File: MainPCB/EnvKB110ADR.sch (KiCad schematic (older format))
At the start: 246 parts, among them SW1 Boot Mode, SW2 Reset Switch, U1 XC6206PxxxMR, U2 STM32F411CEUx, Y1 3225_4P 32.768khz

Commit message: Converted board from STM32F411CEU6 to RP2040
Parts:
- removed C1, C2, C3, C4: 100nf capacitor, Capacitor_SMD:C_0402_1005Metric, symbol Device:C_Small
- removed C10, C9: 0402 22pF, Capacitor_SMD:C_0402_1005Metric, symbol Device:C_Small
- removed C5, C6: 1uf capacitor, Capacitor_SMD:C_0402_1005Metric, symbol Device:C_Small
- removed C7, C8: 100nf 0402, Capacitor_SMD:C_0402_1005Metric, symbol Device:C_Small
- removed R1: 1.5K 0402, Resistor_SMD:R_0402_1005Metric, symbol Device:R_Small
- removed R2: 5.1K 0402, Resistor_SMD:R_0402_1005Metric, symbol Device:R_Small
- removed R3, R4: 22ohm, Resistor_SMD:R_0402_1005Metric, symbol Device:R_Small
- removed R7: 10K 0402, Resistor_SMD:R_0402_1005Metric, symbol Device:R_Small
- removed SW1: Boot Mode, Button_Switch_SMD:Panasonic_EVQPUJ_EVQPUA, symbol Switch:SW_Push
- removed SW2: Reset Switch, Button_Switch_SMD:Panasonic_EVQPUJ_EVQPUA, symbol Switch:SW_Push
- removed U1: XC6206PxxxMR, Package_TO_SOT_SMD:SOT-23, symbol Regulator_Linear:XC6206PxxxMR
- removed U2: STM32F411CEUx, Package_DFN_QFN:QFN-48-1EP_7x7mm_P0.5mm_EP5.6x5.6mm, symbol MCU_ST_STM32F4:STM32F411CEUx
- added C1: 10uf 0603 6.3V, Capacitor_SMD:C_0603_1608Metric, symbol Device:C
- added C10, C3: 1uf 0402, Capacitor_SMD:C_0402_1005Metric, symbol Device:C
- added C11, C13, C14, C15, C16, C18, C5, C6, C7, C8: 100nf 0402, Capacitor_SMD:C_0402_1005Metric, symbol Device:C
- added C17, C4, CBP1: 10uf 0402, Capacitor_SMD:C_0402_1005Metric, symbol Device:C
- added C19, C2: 22pf 0402, Capacitor_SMD:C_0402_1005Metric, symbol Device:C
- added D1: 1N4002W, Diode_SMD:D_SOD-123, symbol Device:D_Schottky
- added D3: LED_0603, LED_SMD:LED_0603_1608Metric, symbol Device:LED
- added FLASH1: W25Q128JVPIQ, Package_SON:WSON-8-1EP_6x5mm_P1.27mm_EP3.4x4mm, symbol W25Q256JVEIQ_TR:W25Q256JVEIQ_TR
- added J2: EVQPU, Button_Switch_SMD:Panasonic_EVQPUJ_EVQPUA, symbol Switch:SW_Push
- added J5: Conn_01x03_Male, Connector_PinHeader_2.54mm:PinHeader_1x03_P2.54mm_Horizontal, symbol Connector_Generic:Conn_01x03
- added PWRLED1: LED_0805, LED_SMD:LED_0805_2012Metric, symbol Device:LED
- added R1, R11: 1K 0402 Resistor, Capacitor_SMD:C_0402_1005Metric, symbol Device:R
- added R10: 1 0402, Resistor_SMD:R_0402_1005Metric, symbol Device:R_Small
- added R12: 1K 0402 Resistor, Resistor_SMD:R_0402_1005Metric, symbol Device:R
- added R2: DNF, Capacitor_SMD:C_0402_1005Metric, symbol Device:R
- added R3, R4: 27 0402 Resistor, Resistor_SMD:R_0402_1005Metric, symbol Device:R
- added R7: 100K 0402 resistor, Resistor_SMD:R_0402_1005Metric, symbol Device:R
- added R8: 470 0402 Resistor, Resistor_SMD:R_0402_1005Metric, symbol Device:R
- added R9: 200 0603, Resistor_SMD:R_0603_1608Metric, symbol Device:R_Small
- added RSW1: EVQPU, Button_Switch_SMD:Panasonic_EVQPUJ_EVQPUA, symbol Device:Jumper_NO_Small
- added TP1, TP2, TP3, TP4, TP5, TP6, TP7, TP8: TestPoint, TestPoint:TestPoint_Pad_D1.0mm, symbol Connector:TestPoint
- added U1: TLV75533PDBVR, Package_TO_SOT_SMD:SOT-23-5, symbol Regulator_Linear:AP131-15
- added U3: RP2040, RP2040_minimal:RP2040-QFN-56, symbol MCU_RaspberryPi_RP2040:RP2040
- R5: LCSC (none) -> (none)
- R6: value 100k 0402 -> 5.1K 0402; LCSC (none) -> (none)
- USB1: value HRO-TYPE-C-31-M-12 -> TYPE-C-31-M-12; footprint Type-C:HRO-TYPE-C-31-M-12-Assembly -> HRO-TYPE-C31-M-12:HRO-TYPE-C-31-M-12; LCSC (none) -> C165948
- Y1: value 3225_4P 32.768khz -> 3225_4P; LCSC (none) -> (none)
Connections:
- net boot0 is gone; now on net GND: R6.1
- net +3V3: now also C10.1, C11.1, C13.1, C14.1, C15.1, C16.1, C17.1, C18.1, C4.1, C5.1, C8.1, FLASH1.8 (VCC), R10.2, R2.1, R9.1, TP6.1, TP8.1, U1.5 (OUT), U3.1 (IOVDD), U3.10 (IOVDD), U3.22 (IOVDD), U3.33 (IOVDD), U3.42 (IOVDD), U3.43 (ADC_AVDD), U3.44 (VREG_IN), U3.48 (USB_VDD), U3.49 (IOVDD)
- net GND: now also C1.2, C10.2, C11.2, C13.2, C14.2, C15.2, C16.2, C17.2, C18.2, C19.1, C2.1, C3.2, C4.2, C5.2, C6.2, C7.2, C8.2, CBP1.2, D3.1 (K), FLASH1.4 (GND), FLASH1.9 (EXP), J2.2, J5.2 (Pin_2), PWRLED1.1 (K), RSW1.1, TP3.1, U1.2 (GND), U3.19 (TESTEN), U3.57 (GND); no longer R6.2
- net VBUS: now also D1.2 (A), R12.2, TP4.1
- net XIN: now reaches Y1.1
- net XIN: now also C2.2, U3.20 (XIN)
- net at Y1.3: now also C19.2, R11.2
- net at USB1.10 (CC2): now also R6.2; no longer R5.2
- net at USB1.4 (CC1): now also R5.2
- net D+ renamed USB_D+
- net USB_D+: now also R3.1, TP1.1
- net D- renamed USB_D-
- net USB_D-: now also R4.1, TP2.1
- new net: R4.2, U3.46 (USB_DM)
- new net: R3.2, U3.47 (USB_DP)
- new net: D3.2 (A), R8.1
- new net: CBP1.1, U1.4 (BP)
- new net: PWRLED1.2 (A), R12.1
- new net +1V1: C3.1, C6.1, C7.1, TP7.1, U3.23 (DVDD), U3.45 (VREG_VOUT), U3.50 (DVDD)
- new net 3V3_EN: R7.1, U1.3 (EN)
- new net ADC_VREF: R10.1, R9.2
- new net GPIO0: U3.2 (GPIO0)
- new net GPIO1: U3.3 (GPIO1)
- new net GPIO10: U3.13 (GPIO10)
- new net GPIO11: U3.14 (GPIO11)
- new net GPIO12: U3.15 (GPIO12)
- new net GPIO13: U3.16 (GPIO13)
- new net GPIO14: U3.17 (GPIO14)
- new net GPIO15: U3.18 (GPIO15)
- new net GPIO16: U3.27 (GPIO16)
- new net GPIO17: U3.28 (GPIO17)
- new net GPIO18: U3.29 (GPIO18)
- new net GPIO19: U3.30 (GPIO19)
- new net GPIO2: U3.4 (GPIO2)
- new net GPIO20: U3.31 (GPIO20)
- new net GPIO21: U3.32 (GPIO21)
- new net GPIO22: U3.34 (GPIO22)
- new net GPIO23: U3.35 (GPIO23)
- new net GPIO24: U3.36 (GPIO24)
- new net GPIO25: R8.2, U3.37 (GPIO25)
- new net GPIO26_ADC0: U3.38 (GPIO26_ADC0)
- new net GPIO27_ADC1: U3.39 (GPIO27_ADC1)
- new net GPIO28_ADC2: U3.40 (GPIO28_ADC2)
- new net GPIO29_ADC3: U3.41 (GPIO29_ADC3)
- new net GPIO3: U3.5 (GPIO3)
- new net GPIO4: U3.6 (GPIO4)
- new net GPIO5: U3.7 (GPIO5)
- new net GPIO6: U3.8 (GPIO6)
- new net GPIO7: U3.9 (GPIO7)
- new net GPIO8: U3.11 (GPIO8)
- new net GPIO9: U3.12 (GPIO9)
- new net QSPI_SCLK: FLASH1.6 (CLK), U3.52 (QSPI_SCLK)
- new net QSPI_SD0: FLASH1.5 (DI(IO0)), U3.53 (QSPI_SD0)
- new net QSPI_SD1: FLASH1.2 (DO(IO1)), U3.55 (QSPI_SD1)
- new net QSPI_SD2: FLASH1.3 (IO2), U3.54 (QSPI_SD2)
- new net QSPI_SD3: FLASH1.7 (IO3), U3.51 (QSPI_SD3)
- new net QSPI_SS: FLASH1.1 (~CS), R1.1, R2.2, U3.56 (QSPI_SS)
- new net RUN: RSW1.2, U3.26 (RUN)
- new net SWCLK: J5.1 (Pin_1), U3.24 (SWCLK)
- new net SWD: J5.3 (Pin_3), U3.25 (SWD)
- new net VSYS: C1.1, D1.1 (K), R7.2, TP5.1, U1.1 (IN)
- new net XOUT: R11.1, U3.21 (XOUT)
- new net ~USB_BOOT: J2.1, R1.2
- no-connect marks 7 -> 3
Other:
- note added: "2x 5.1K Resistors on the CC pins will = 5V@1.5A\nthis is the recomended default config for type-c"
- note added: "Crystal"
- note added: "D1 NEEDS to be 0omh resistor or 1N4002 diode"
- note added: "DO.NOT.FIT"
- note added: "Flash"
- note added: "GD25Q40CEIGR is compatible and often stocked by JLC"
- note added: "Im pretty sure a lot of these W25QXXX Chips are pin compatible\nDont quote me on that"
- note added: "Im unsure if the RP2040 can function with flash larger than 128Mb"
- note added: "KoreanHROParts \nUSB_C_Receptacle_HRO_TYPE-C-31-M-12"
- note added: "MAKE SURE THIS LINE is ran off of pin43\nor close to pin43"
- note added: "Make sure C10 is close to pin 44 of RP2040"
- note added: "Make sure C3 is close to pin 45 of RP2040"
- note added: "Make sure R3 and R4 are close to RP2040"
- note added: "Only fit cBP1 if you have selected an \nalternate voltage regulator\n\nTLV75533PDBVR does not."
- note added: "Pin 9 technically doesnt exist\nits the main central contact under\nthe chip for heat dicipation"
- note added: "RP2040 supports 1MHz to 15MHz"
- note added: "Test points"
- note added: "These decoupling capacitors are meant\nto be put close by each 3.3V pin of the RP2040"
- note added: "USB/POWER"
- note added: "place one by the CPU\nand one by the regulator\n(3.3V Test points)"
- note added: "this is for factory testing\nalways pull this to ground"
- note removed: "these capacitors should all be placed\n near the power pin of the STM32"
- note removed: "unsure what this pullup resistor is for\nbut its used in some MCU boards so lets copy it"
- moved on the sheet: D_100, D_101, D_102, D_103, D_104, D_105, D_106, D_107, D_108, D_109, D_110, D_111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

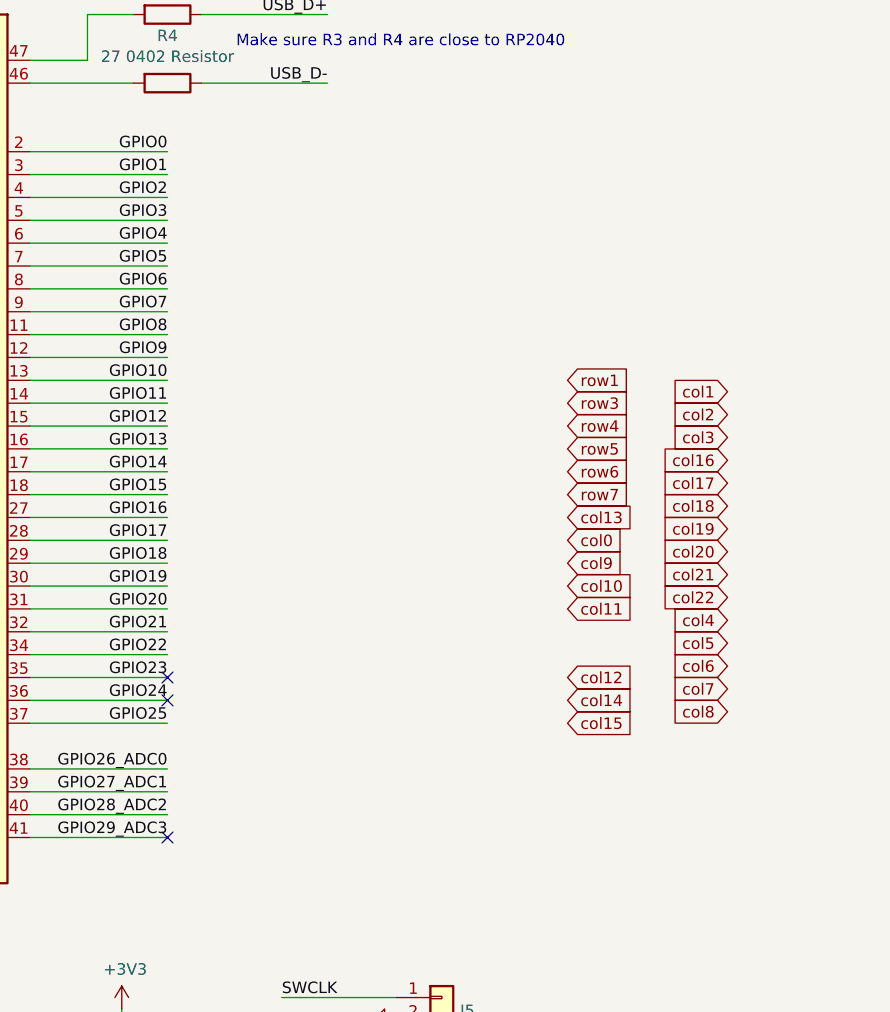
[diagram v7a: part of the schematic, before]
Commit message: wired up all the traces required to make the keyboard functional.
However this means you can no longer use the Rpi pico firmware with this and needs a custom compiled firmware to utilize the normally unavailable pins,
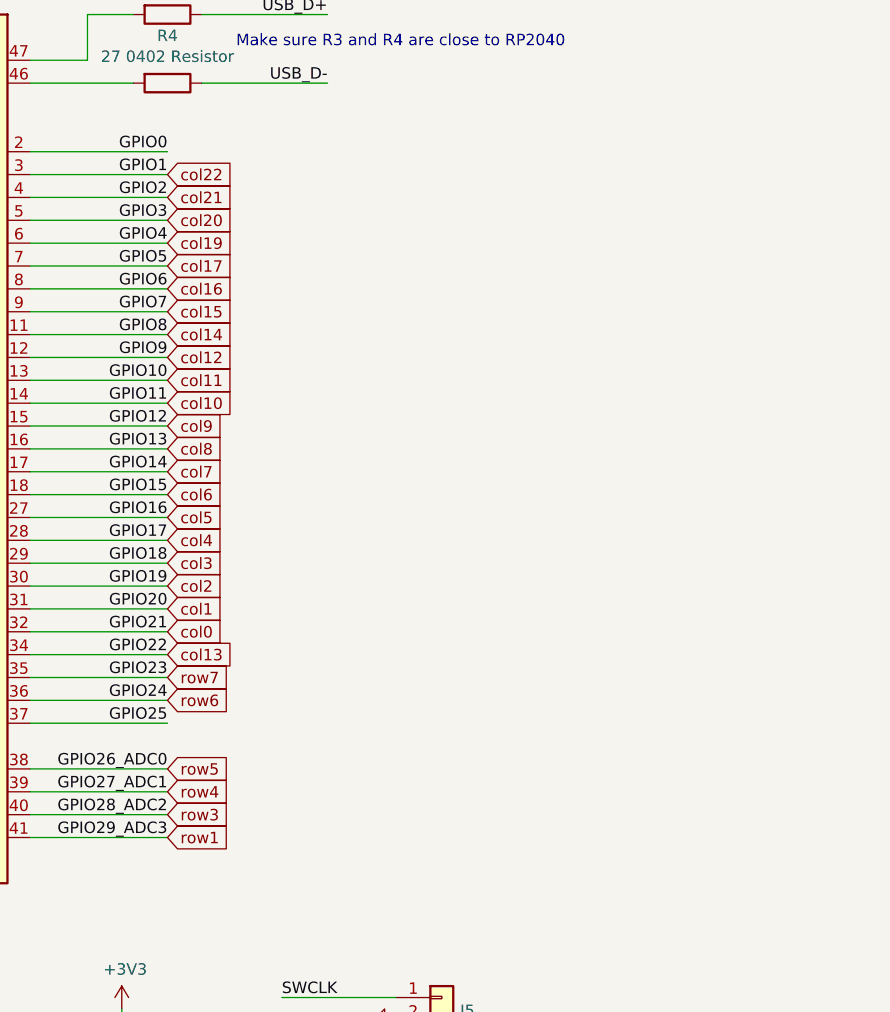
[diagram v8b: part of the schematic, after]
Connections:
- net GPIO1 is gone; now on net col22: U3.3 (GPIO1)
- net GPIO10 is gone; now on net col11: U3.13 (GPIO10)
- net GPIO11 is gone; now on net col10: U3.14 (GPIO11)
- net GPIO12 is gone; now on net col9: U3.15 (GPIO12)
- net GPIO13 is gone; now on net col8: U3.16 (GPIO13)
- net GPIO14 is gone; now on net col7: U3.17 (GPIO14)
- net GPIO15 is gone; now on net col6: U3.18 (GPIO15)
- net GPIO16 is gone; now on net col5: U3.27 (GPIO16)
- net GPIO17 is gone; now on net col4: U3.28 (GPIO17)
- net GPIO18 is gone; now on net col3: U3.29 (GPIO18)
- net GPIO19 is gone; now on net col2: U3.30 (GPIO19)
- net GPIO2 is gone; now on net col21: U3.4 (GPIO2)
- net GPIO20 is gone; now on net col1: U3.31 (GPIO20)
- net GPIO21 is gone; now on net col0: U3.32 (GPIO21)
- net GPIO22 is gone; now on net col13: U3.34 (GPIO22)
- net GPIO23 is gone; now on net row7: U3.35 (GPIO23)
- net GPIO24 is gone; now on net row6: U3.36 (GPIO24)
- net GPIO26_ADC0 is gone; now on net row5: U3.38 (GPIO26_ADC0)
- net GPIO27_ADC1 is gone; now on net row4: U3.39 (GPIO27_ADC1)
- net GPIO28_ADC2 is gone; now on net row3: U3.40 (GPIO28_ADC2)
- net GPIO29_ADC3 is gone; now on net row1: U3.41 (GPIO29_ADC3)
- net GPIO3 is gone; now on net col20: U3.5 (GPIO3)
- net GPIO4 is gone; now on net col19: U3.6 (GPIO4)
- net GPIO5 is gone; now on net col17: U3.7 (GPIO5)
- net GPIO6 is gone; now on net col16: U3.8 (GPIO6)
- net GPIO7 is gone; now on net col15: U3.9 (GPIO7)
- net GPIO8 is gone; now on net col14: U3.11 (GPIO8)
- net GPIO9 is gone; now on net col12: U3.12 (GPIO9)
- no-connect marks 3 -> 0
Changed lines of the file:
@@
 	1    0    0    -1
 $EndComp
-Text GLabel 11400 6100 2    50   Input ~ 0
+Text GLabel 9650 6500 2    50   Input ~ 0
 col0
-Text GLabel 12100 5450 0    50   Input ~ 0
+Text GLabel 9650 6400 2    50   Input ~ 0
 col1
-Text GLabel 12100 5550 0    50   Input ~ 0
+Text GLabel 9650 6300 2    50   Input ~ 0
 col2
-Text GLabel 12100 5650 0    50   Input ~ 0
+Text GLabel 9650 6200 2    50   Input ~ 0
 col3
-Text GLabel 12100 6450 0    50   Input ~ 0
+Text GLabel 9650 6100 2    50   Input ~ 0
 col4
-Text GLabel 12100 6550 0    50   Input ~ 0
+Text GLabel 9650 6000 2    50   Input ~ 0
 col5
-Text GLabel 12100 6650 0    50   Input ~ 0
+Text GLabel 9650 5900 2    50   Input ~ 0
 col6
-Text GLabel 12100 6750 0    50   Input ~ 0
+Text GLabel 9650 5800 2    50   Input ~ 0
 col7
-Text GLabel 12100 6850 0    50   Input ~ 0
+Text GLabel 9650 5700 2    50   Input ~ 0
 col8
-Text GLabel 11400 6200 2    50   Input ~ 0
+Text GLabel 9650 5600 2    50   Input ~ 0
 col9
-Text GLabel 11400 6300 2    50   Input ~ 0
+Text GLabel 9650 5500 2    50   Input ~ 0
 col10
-Text GLabel 11400 6400 2    50   Input ~ 0
+Text GLabel 9650 5400 2    50   Input ~ 0
 col11
-Text GLabel 11400 6700 2    50   Input ~ 0
+Text GLabel 9650 5300 2    50   Input ~ 0
 col12
-Text GLabel 11400 6000 2    50   Input ~ 0
+Text GLabel 9650 6600 2    50   Input ~ 0
 col13
-Text GLabel 11400 6800 2    50   Input ~ 0
+Text GLabel 9650 5200 2    50   Input ~ 0
 col14
-Text GLabel 11400 6900 2    50   Input ~ 0
+Text GLabel 9650 5100 2    50   Input ~ 0
 col15
-Text GLabel 12100 5750 0    50   Input ~ 0
+Text GLabel 9650 5000 2    50   Input ~ 0
 col16
-Text GLabel 12100 5850 0    50   Input ~ 0
+Text GLabel 9650 4900 2    50   Input ~ 0
 col17
-Text GLabel 12100 5950 0    50   Input ~ 0
-col18
-Text GLabel 12100 6050 0    50   Input ~ 0
+Text GLabel 9650 4800 2    50   Input ~ 0
 col19
-Text GLabel 12100 6150 0    50   Input ~ 0
+Text GLabel 9650 4700 2    50   Input ~ 0
 col20
-Text GLabel 12100 6250 0    50   Input ~ 0
+Text GLabel 9650 4600 2    50   Input ~ 0
 col21
-Text GLabel 12100 6350 0    50   Input ~ 0
+Text GLabel 9650 4500 2    50   Input ~ 0
 col22
-Text GLabel 11400 5400 2    50   Input ~ 0
+Text GLabel 9650 7400 2    50   Input ~ 0
 row1
-Text GLabel 11400 5500 2    50   Input ~ 0
+Text GLabel 9650 7300 2    50   Input ~ 0
 row3
-Text GLabel 11400 5600 2    50   Input ~ 0
+Text GLabel 9650 7200 2    50   Input ~ 0
 row4
-Text GLabel 11400 5700 2    50   Input ~ 0
+Text GLabel 9650 7100 2    50   Input ~ 0
 row5
-Text GLabel 11400 5800 2    50   Input ~ 0
+Text GLabel 9650 6800 2    50   Input ~ 0
 row6
-Text GLabel 11400 5900 2    50   Input ~ 0
+Text GLabel 9650 6700 2    50   Input ~ 0
 row7
 Connection ~ 15950 19100
@@
 Wire Wire Line
 	10600 8800 10700 8800
-NoConn ~ 9650 7400
-NoConn ~ 9650 6700
-NoConn ~ 9650 6800
 $Comp
 L Device:C C5
